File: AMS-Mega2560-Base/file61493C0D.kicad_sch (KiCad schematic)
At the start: 50 parts, among them IC10 LM2597MX-ADJ_NOPB, IC11 LM2597M-3.3_NOPB, IC12 OPA2340PA, IC9 LM2670SX-5.0_NOPB, J21 Screw_Terminal_01x03, J22 Conn_01x07, Q21 IRF9Z34NPBF, Q22 BD140, Q23 2N7000, Q5 2N7000, Q6 IRF9Z34NPBF, U1 BK_HTC-15M, U2 TL431LP

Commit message: pushing this change to the repo need to vet some schematics
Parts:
- removed Q22: BD140, Package_TO_SOT_THT:TO-126-3_Vertical, symbol Transistor_BJT:BD140
- added Q22: IRF9610PBF-BE3, TO254P465X1024X2050-3P, symbol Samac_Sys:IRF9610PBF-BE3
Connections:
- net +3.3VA: now also Q22.2
- net +3.3VP: now also Q22.3
- net at R63.1: now also Q22.1
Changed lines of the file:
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@@
   (junction (at 236.22 123.19) (diameter 0) (color 0 0 0 0)
   )
-  (junction (at 84.455 192.405) (diameter 0) (color 0 0 0 0)
+  (junction (at 84.455 197.485) (diameter 0) (color 0 0 0 0)
   )
   (junction (at 90.17 104.775) (diameter 0) (color 0 0 0 0)
@@
     (stroke (width 0) (type default) (color 0 0 0 0))
   )
-  (wire (pts (xy 78.74 194.31) (xy 84.455 194.31))
+  (wire (pts (xy 78.74 199.39) (xy 84.455 199.39))
     (stroke (width 0) (type default) (color 0 0 0 0))
   )
@@
     (stroke (width 0) (type default) (color 0 0 0 0))
   )
-  (wire (pts (xy 84.455 186.055) (xy 84.455 192.405))
+  (wire (pts (xy 84.455 191.135) (xy 84.455 197.485))
     (stroke (width 0) (type default) (color 0 0 0 0))
   )
@@
     (stroke (width 0) (type default) (color 0 0 0 0))
   )
-  (wire (pts (xy 84.455 194.31) (xy 84.455 192.405))
+  (wire (pts (xy 84.455 199.39) (xy 84.455 197.485))
     (stroke (width 0) (type default) (color 0 0 0 0))
   )
@@
     (stroke (width 0) (type default) (color 0 0 0 0))
   )
-  (wire (pts (xy 87.63 192.405) (xy 87.63 190.5))
+  (wire (pts (xy 87.63 197.485) (xy 87.63 195.58))
     (stroke (width 0) (type default) (color 0 0 0 0))
   )
@@
     (stroke (width 0) (type default) (color 0 0 0 0))
   )
-  (wire (pts (xy 84.455 192.405) (xy 87.63 192.405))
+  (wire (pts (xy 84.455 197.485) (xy 87.63 197.485))
     (stroke (width 0) (type default) (color 0 0 0 0))
   )
@@
     (pin "3")
   )
-  (symbol (lib_id "Transistor_BJT:BD140") (at 81.915 180.975 0) (mirror x) (unit 1)
-    (in_bom yes) (on_board yes) (fields_autoplaced)
-    (property "Reference" "Q22" (id 0) (at 86.7918 180.0665 0)
-      (effects (font (size 1.27 1.27)) (justify left))
-    )
-    (property "Value" "BD140" (id 1) (at 86.7918 182.8416 0)
-      (effects (font (size 1.27 1.27)) (justify left))
-    )
-    (property "Footprint" "Package_TO_SOT_THT:TO-126-3_Vertical" (id 2) (at 86.995 179.07 0)
-      (effects (font (size 1.27 1.27) italic) (justify left) hide)
-    )
-    (property "Datasheet" "http://www.st.com/internet/com/TECHNICAL_RESOURCES/TECHNICAL_LITERATURE/DATASHEET/CD00001225.pdf" (id 3) (at 81.915 180.975 0)
-      (effects (font (size 1.27 1.27)) (justify left) hide)
-    )
-    (pin "1")
-    (pin "2")
-    (pin "3")
-  )
   (symbol (lib_id "power:PWR_FLAG") (at 267.97 40.005 0) (unit 1)
     (in_bom yes) (on_board yes) (fields_autoplaced)
@@
     (pin "2")
   )
-  (symbol (lib_id "power:PWR_FLAG") (at 78.74 194.31 0) (unit 1)
+  (symbol (lib_id "power:PWR_FLAG") (at 78.74 199.39 0) (unit 1)
     (in_bom yes) (on_board yes) (fields_autoplaced)
-    (property "Reference" "#FLG01" (id 0) (at 78.74 192.405 0)
-      (effects (font (size 1.27 1.27)) hide)
-    )
-    (property "Value" "PWR_FLAG" (id 1) (at 78.74 190.7055 0))
-    (property "Footprint" "" (id 2) (at 78.74 194.31 0)
-      (effects (font (size 1.27 1.27)) hide)
-    )
-    (property "Datasheet" "~" (id 3) (at 78.74 194.31 0)
+    (property "Reference" "#FLG01" (id 0) (at 78.74 197.485 0)
+      (effects (font (size 1.27 1.27)) hide)
+    )
+    (property "Value" "PWR_FLAG" (id 1) (at 78.74 195.7855 0))
+    (property "Footprint" "" (id 2) (at 78.74 199.39 0)
+      (effects (font (size 1.27 1.27)) hide)
+    )
+    (property "Datasheet" "~" (id 3) (at 78.74 199.39 0)
       (effects (font (size 1.27 1.27)) hide)
     )
@@
     (pin "1")
   )
+  (symbol (lib_id "Samac_Sys:IRF9610PBF-BE3") (at 76.835 180.975 0) (mirror x) (unit 1)
+    (in_bom yes) (on_board yes) (fields_autoplaced)
+    (property "Reference" "Q22" (id 0) (at 87.757 182.6065 0)
+      (effects (font (size 1.27 1.27)) (justify left))
+    )
+    (property "Value" "IRF9610PBF-BE3" (id 1) (at 87.757 185.3816 0)
+      (effects (font (size 1.27 1.27)) (justify left))
+    )
+    (property "Footprint" "TO254P465X1024X2050-3P" (id 2) (at 88.265 179.705 0)
+      (effects (font (size 1.27 1.27)) (justify left) hide)
+    )
+    (property "Datasheet" "" (id 3) (at 88.265 177.165 0)
+      (effects (font (size 1.27 1.27)) (justify left) hide)
+    )
+    (property "Description" "MOSFET 200V P-CH HEXFET MOSFET" (id 4) (at 88.265 174.625 0)
+      (effects (font (size 1.27 1.27)) (justify left) hide)
+    )
+    (property "Height" "4.65" (id 5) (at 88.265 172.085 0)
+      (effects (font (size 1.27 1.27)) (justify left) hide)
+    )
+    (property "Mouser Part Number" "78-IRF9610PBF-BE3" (id 6) (at 88.265 169.545 0)
+      (effects (font (size 1.27 1.27)) (justify left) hide)
+    )
+    (property "Mouser Price/Stock" "https://www.mouser.co.uk/ProductDetail/Vishay-Siliconix/IRF9610PBF-BE3?qs=zW32dvEIR3so9ERRF7EoZg%3D%3D" (id 7) (at 88.265 167.005 0)
+      (effects (font (size 1.27 1.27)) (justify left) hide)
+    )
+    (property "Manufacturer_Name" "Vishay" (id 8) (at 88.265 164.465 0)
+      (effects (font (size 1.27 1.27)) (justify left) hide)
+    )
+    (property "Manufacturer_Part_Number" "IRF9610PBF-BE3" (id 9) (at 88.265 161.925 0)
+      (effects (font (size 1.27 1.27)) (justify left) hide)
+    )
+    (pin "1")
+    (pin "2")
+    (pin "3")
+  )
   (symbol (lib_id "power:PWR_FLAG") (at 33.02 76.835 0) (unit 1)
     (in_bom yes) (on_board yes) (fields_autoplaced)
@@
     (pin "2")
   )
-  (symbol (lib_id "power:+3.3VA") (at 87.63 190.5 0) (mirror y) (unit 1)
+  (symbol (lib_id "power:+3.3VA") (at 87.63 195.58 0) (mirror y) (unit 1)
     (in_bom yes) (on_board yes) (fields_autoplaced)
-    (property "Reference" "#PWR096" (id 0) (at 87.63 194.31 0)
-      (effects (font (size 1.27 1.27)) hide)
-    )
-    (property "Value" "+3.3VA" (id 1) (at 87.63 186.8955 0))
-    (property "Footprint" "" (id 2) (at 87.63 190.5 0)
-      (effects (font (size 1.27 1.27)) hide)
-    )
-    (property "Datasheet" "" (id 3) (at 87.63 190.5 0)
-      (effects (font (size 1.27 1.27)) hide)
-    )
+    (property "Reference" "#PWR096" (id 0) (at 87.63 199.39 0)
+      (effects (font (size 1.27 1.27)) hide)
+    )
+    (property "Value" "+3.3VA" (id 1) (at 87.63 191.9755 0))
+    (property "Footprint" "" (id 2) (at 87.63 195.58 0)
+      (effects (font (size 1.27 1.27)) hide)
+    )
+    (property "Datasheet" "" (id 3) (at 87.63 195.58 0)
+      (effects (font (size 1.27 1.27)) hide)
+    )

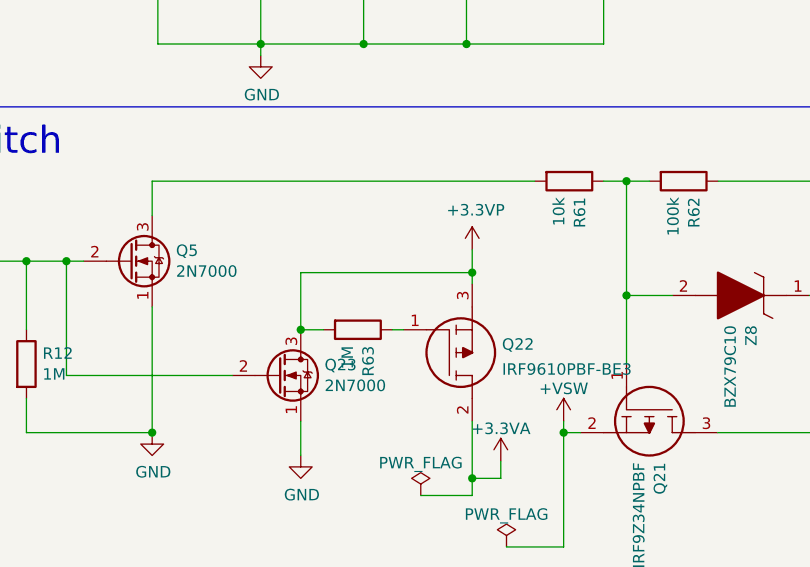
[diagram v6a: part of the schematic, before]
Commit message: removing separate project for lack of chips and switching to dev boards. copied out the schematics used.
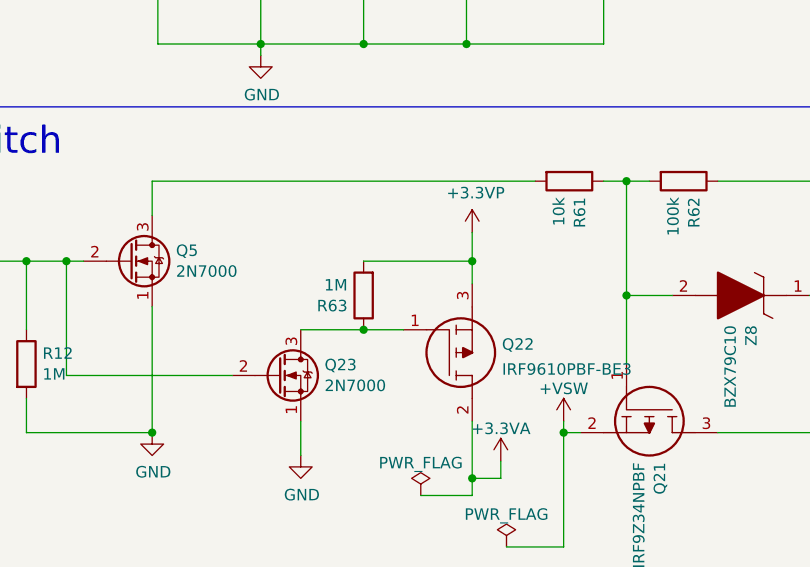
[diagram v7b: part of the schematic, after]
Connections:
- net +3.3VP: no longer Q23.3 (D)
- net at Q22.1, R63.1: now also Q23.3 (D)
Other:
- moved on the sheet: R63
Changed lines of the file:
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@@
   (junction (at 34.925 173.355) (diameter 0) (color 0 0 0 0)
   )
+  (junction (at 84.455 173.355) (diameter 0) (color 0 0 0 0)
+  )
   (junction (at 273.05 47.625) (diameter 0) (color 0 0 0 0)
   )
@@
   (junction (at 191.77 60.96) (diameter 0) (color 0 0 0 0)
   )
-  (junction (at 84.455 174.625) (diameter 0) (color 0 0 0 0)
-  )
   (junction (at 69.85 125.095) (diameter 0) (color 0 0 0 0)
   )
@@
   (junction (at 72.39 149.225) (diameter 0) (color 0 0 0 0)
   )
+  (junction (at 72.39 180.975) (diameter 0) (color 0 0 0 0)
+  )
   (junction (at 241.3 142.24) (diameter 0) (color 0 0 0 0)
   )
@@
   )
   (junction (at 48.895 192.405) (diameter 0) (color 0 0 0 0)
-  )
-  (junction (at 65.405 180.975) (diameter 0) (color 0 0 0 0)
   )
   (junction (at 207.01 67.31) (diameter 0) (color 0 0 0 0)
@@
     (stroke (width 0) (type default) (color 0 0 0 0))
   )
-  (wire (pts (xy 84.455 174.625) (xy 84.455 175.895))
+  (wire (pts (xy 84.455 170.18) (xy 84.455 173.355))
     (stroke (width 0) (type default) (color 0 0 0 0))
   )
@@
     (stroke (width 0) (type default) (color 0 0 0 0))
   )
+  (wire (pts (xy 72.39 173.355) (xy 84.455 173.355))
+    (stroke (width 0) (type default) (color 0 0 0 0))
+  )
   (wire (pts (xy 207.01 68.58) (xy 207.01 67.31))
     (stroke (width 0) (type default) (color 0 0 0 0))
@@
     (stroke (width 0) (type default) (color 0 0 0 0))
   )
+  (wire (pts (xy 65.405 180.975) (xy 72.39 180.975))
+    (stroke (width 0) (type default) (color 0 0 0 0))
+  )
   (wire (pts (xy 121.92 50.8) (xy 102.87 50.8))
     (stroke (width 0) (type default) (color 0 0 0 0))
@@
     (stroke (width 0) (type default) (color 0 0 0 0))
   )
+  (wire (pts (xy 84.455 173.355) (xy 84.455 175.895))
+    (stroke (width 0) (type default) (color 0 0 0 0))
+  )
   (wire (pts (xy 271.78 47.625) (xy 273.05 47.625))
     (stroke (width 0) (type default) (color 0 0 0 0))
@@
     (stroke (width 0) (type default) (color 0 0 0 0))
   )
-  (wire (pts (xy 65.405 180.975) (xy 65.405 174.625))
-    (stroke (width 0) (type default) (color 0 0 0 0))
-  )
   (wire (pts (xy 77.47 63.5) (xy 77.47 62.23))
     (stroke (width 0) (type default) (color 0 0 0 0))
@@
     (stroke (width 0) (type default) (color 0 0 0 0))
   )
-  (wire (pts (xy 65.405 174.625) (xy 84.455 174.625))
-    (stroke (width 0) (type default) (color 0 0 0 0))
-  )
   (wire (pts (xy 273.05 47.625) (xy 273.05 43.18))
     (stroke (width 0) (type default) (color 0 0 0 0))
@@
     (stroke (width 0) (type default) (color 0 0 0 0))
   )
-  (wire (pts (xy 67.945 180.975) (xy 65.405 180.975))
-    (stroke (width 0) (type default) (color 0 0 0 0))
-  )
   (wire (pts (xy 102.87 54.61) (xy 95.25 54.61))
     (stroke (width 0) (type default) (color 0 0 0 0))
@@
     (stroke (width 0) (type default) (color 0 0 0 0))
   )
-  (wire (pts (xy 84.455 172.085) (xy 84.455 174.625))
-    (stroke (width 0) (type default) (color 0 0 0 0))
-  )
   (wire (pts (xy 101.6 164.465) (xy 104.14 164.465))
     (stroke (width 0) (type default) (color 0 0 0 0))
@@
     (stroke (width 0) (type default) (color 0 0 0 0))
   )
-  (wire (pts (xy 75.565 180.975) (xy 76.835 180.975))
+  (wire (pts (xy 72.39 180.975) (xy 76.835 180.975))
     (stroke (width 0) (type default) (color 0 0 0 0))
   )
@@
     (pin "3")
   )
-  (symbol (lib_id "Device:R") (at 71.755 180.975 270) (unit 1)
-    (in_bom yes) (on_board yes)
-    (property "Reference" "R63" (id 0) (at 72.9234 182.753 0)
-      (effects (font (size 1.27 1.27)) (justify left))
-    )
-    (property "Value" "1M" (id 1) (at 70.612 182.753 0)
-      (effects (font (size 1.27 1.27)) (justify left))
-    )
-    (property "Footprint" "Resistor_THT:R_Axial_DIN0207_L6.3mm_D2.5mm_P2.54mm_Vertical" (id 2) (at 71.755 179.197 90)
-      (effects (font (size 1.27 1.27)) hide)
-    )
-    (property "Datasheet" "~" (id 3) (at 71.755 180.975 0)
+  (symbol (lib_id "Device:R") (at 72.39 177.165 180) (unit 1)
+    (in_bom yes) (on_board yes)
+    (property "Reference" "R63" (id 0) (at 70.612 178.3334 0)
+      (effects (font (size 1.27 1.27)) (justify left))
+    )
+    (property "Value" "1M" (id 1) (at 70.612 176.022 0)
+      (effects (font (size 1.27 1.27)) (justify left))
+    )
+    (property "Footprint" "Resistor_THT:R_Axial_DIN0207_L6.3mm_D2.5mm_P2.54mm_Vertical" (id 2) (at 74.168 177.165 90)
+      (effects (font (size 1.27 1.27)) hide)
+    )
+    (property "Datasheet" "~" (id 3) (at 72.39 177.165 0)
       (effects (font (size 1.27 1.27)) hide)
     )
@@
     (pin "1")
   )
-  (symbol (lib_id "power:+3.3VP") (at 84.455 172.085 0) (unit 1)
-    (in_bom yes) (on_board yes)
-    (property "Reference" "#PWR093" (id 0) (at 88.265 173.355 0)
-      (effects (font (size 1.27 1.27)) hide)
-    )
-    (property "Value" "+3.3VP" (id 1) (at 84.836 167.6908 0))
-    (property "Footprint" "" (id 2) (at 84.455 172.085 0)
-      (effects (font (size 1.27 1.27)) hide)
-    )
-    (property "Datasheet" "" (id 3) (at 84.455 172.085 0)
-      (effects (font (size 1.27 1.27)) hide)
-    )
+  (symbol (lib_id "power:+3.3VP") (at 84.455 170.18 0) (unit 1)
+    (in_bom yes) (on_board yes)
+    (property "Reference" "#PWR093" (id 0) (at 88.265 171.45 0)
+      (effects (font (size 1.27 1.27)) hide)
+    )
+    (property "Value" "+3.3VP" (id 1) (at 84.836 165.7858 0))
+    (property "Footprint" "" (id 2) (at 84.455 170.18 0)
+      (effects (font (size 1.27 1.27)) hide)
+    )
+    (property "Datasheet" "" (id 3) (at 84.455 170.18 0)
+      (effects (font (size 1.27 1.27)) hide)
+    )

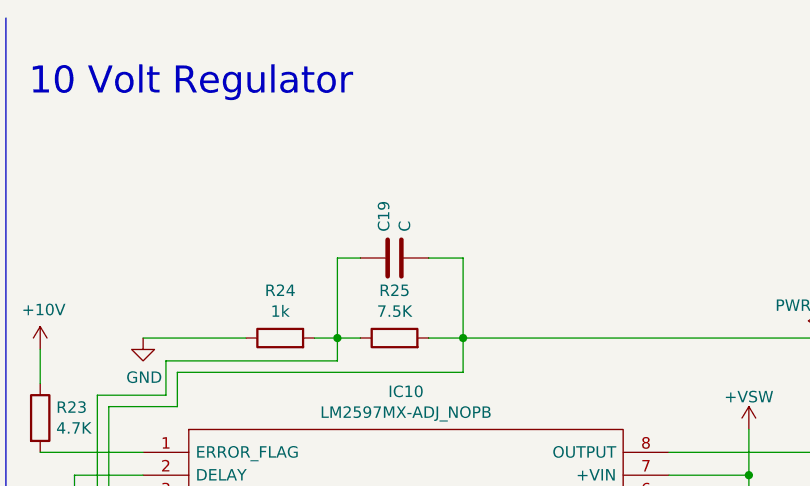
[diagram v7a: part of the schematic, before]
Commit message: applying some fixes for the RPM sensor and other parts of the schem
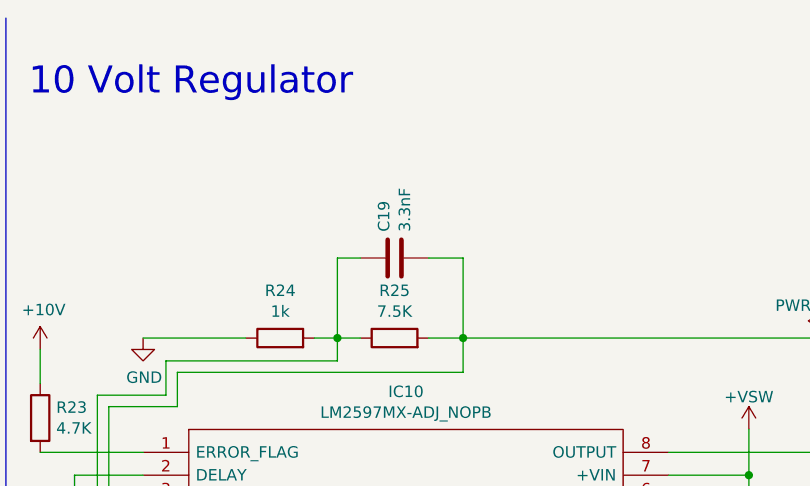
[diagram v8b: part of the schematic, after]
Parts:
- C19: value C -> 3.3nF
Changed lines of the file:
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@@
       (effects (font (size 1.27 1.27)) (justify left))
     )
-    (property "Value" "C" (id 1) (at 129.413 36.449 0)
+    (property "Value" "3.3nF" (id 1) (at 129.413 36.449 0)
       (effects (font (size 1.27 1.27)) (justify left))
     )
